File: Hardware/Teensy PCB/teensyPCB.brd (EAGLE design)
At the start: 100 x 50 mm, 14 parts, among them U2 USD-SOCKETNEW

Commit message: Created library component for digipot
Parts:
- added U$5: DIGIPOT, DigiPot:SOT23-8L
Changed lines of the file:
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@@
 <?xml version="1.0" encoding="utf-8"?>
 <!DOCTYPE eagle SYSTEM "eagle.dtd">
-<eagle version="7.4.0">
+<eagle version="7.2.0">
 <drawing>
 <settings>
@@
 <layers>
 <layer number="1" name="Top" color="4" fill="1" visible="yes" active="yes"/>
+<layer number="2" name="Route2" color="1" fill="3" visible="no" active="no"/>
+<layer number="3" name="Route3" color="4" fill="3" visible="no" active="no"/>
+<layer number="4" name="Route4" color="1" fill="4" visible="no" active="no"/>
+<layer number="5" name="Route5" color="4" fill="4" visible="no" active="no"/>
+<layer number="6" name="Route6" color="1" fill="8" visible="no" active="no"/>
+<layer number="7" name="Route7" color="4" fill="8" visible="no" active="no"/>
+<layer number="8" name="Route8" color="1" fill="2" visible="no" active="no"/>
+<layer number="9" name="Route9" color="4" fill="2" visible="no" active="no"/>
+<layer number="10" name="Route10" color="1" fill="7" visible="no" active="no"/>
+<layer number="11" name="Route11" color="4" fill="7" visible="no" active="no"/>
+<layer number="12" name="Route12" color="1" fill="5" visible="no" active="no"/>
+<layer number="13" name="Route13" color="4" fill="5" visible="no" active="no"/>
+<layer number="14" name="Route14" color="1" fill="6" visible="no" active="no"/>
+<layer number="15" name="Route15" color="4" fill="6" visible="no" active="no"/>
 <layer number="16" name="Bottom" color="1" fill="1" visible="yes" active="yes"/>
 <layer number="17" name="Pads" color="2" fill="1" visible="yes" active="yes"/>
@@
 <element name="U2" library="SparkFun-Connectors" package="MICRO-SD-SOCKET-PP" value="USD-SOCKETNEW" x="43.71" y="21.59"/>
 <element name="J_ULTRASONIC_2" library="HC-SR04" package="HC-SR04_FOOTPRINT" value="HC-SR04" x="43.77" y="8.2" rot="R90"/>
+<element name="U$5" library="DigiPot" package="SOT23-8L" value="DIGIPOT" x="-4" y="2"/>
 </elements>
 <signals>

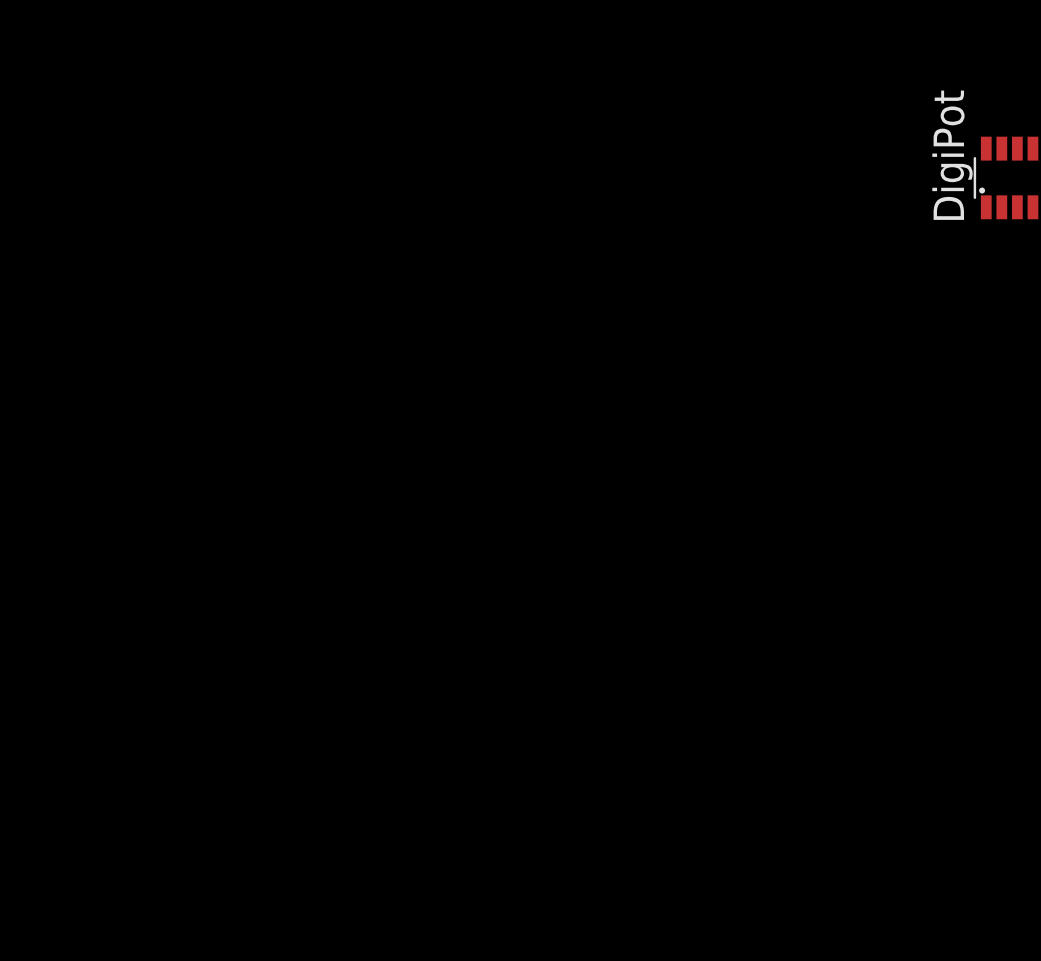
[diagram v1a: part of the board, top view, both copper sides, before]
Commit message: Wired digipot, added push buttons with voltage debounce, updated audio amplifier
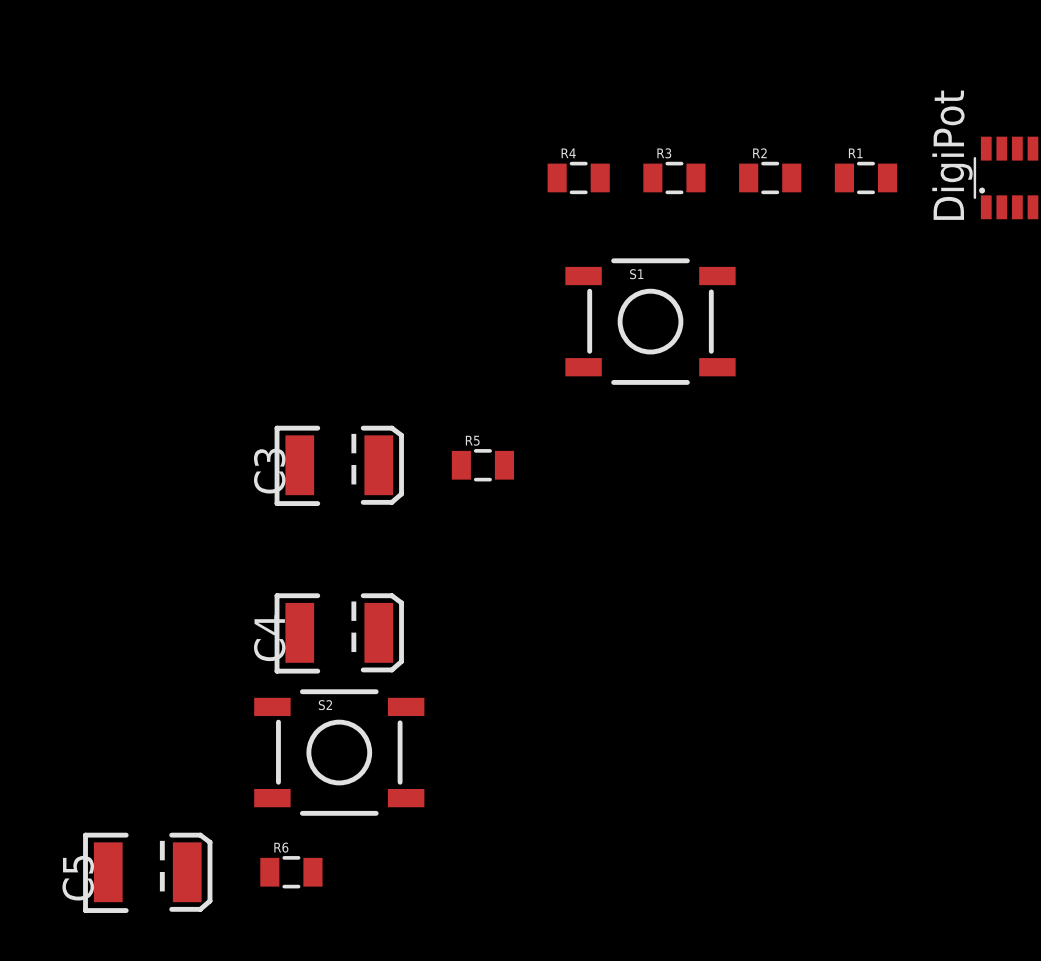
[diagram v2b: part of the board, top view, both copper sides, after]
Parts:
- added C3, C4: 100nF, SparkFun-Capacitors:EIA3528
- added C5: 10uF, SparkFun-Capacitors:EIA3528
- added R1, R2, R3, R4: 4.7k, SparkFun-Resistors:0805
- added R5, R6: 10k, SparkFun-Resistors:0805
- added S1, S2: TAC_SWITCHSMD, SparkFun-Retired:TACTILE-SWITCH-SMD
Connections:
- removed net VUSB: U$1.VUSB
- new net N$2: C4.C, R6.2, S2.3, S2.4, U$1.A11
- new net N$3: C5.C, U$5.A
- new net N$9: C3.C, R5.2, S1.3, S1.4, U$1.A12
- new net SW: U$1.A13, U$4.SW
- new net WOUT: C2.A, U$5.W
- net 5V: now also C3.A, C4.A, R1.2, R2.2, R3.2, R4.2, S1.1, S1.2, S2.1, S2.2, U$1.VUSB, U$5.VDD
- net DAC: now also C5.A; no longer C2.A
- net GND: now also R5.1, R6.1, U$5.AD0, U$5.B, U$5.GND
- net SCL0: now also R2.1, U$5.SCL
- net SCL1: now also R4.1
- net SDA0: now also R1.1, U$5.SDA
- net SDA1: now also R3.1
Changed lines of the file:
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@@
 <element name="J_ULTRASONIC_2" library="HC-SR04" package="HC-SR04_FOOTPRINT" value="HC-SR04" x="43.77" y="8.2" rot="R90"/>
 <element name="U$5" library="DigiPot" package="SOT23-8L" value="DIGIPOT" x="-4" y="2"/>
+<element name="R1" library="SparkFun-Resistors" package="0805" value="4.7k" x="-10" y="2"/>
+<element name="R2" library="SparkFun-Resistors" package="0805" value="4.7k" x="-14" y="2"/>
+<element name="R3" library="SparkFun-Resistors" package="0805" value="4.7k" x="-18" y="2"/>
+<element name="R4" library="SparkFun-Resistors" package="0805" value="4.7k" x="-22" y="2"/>
+<element name="S1" library="SparkFun-Retired" package="TACTILE-SWITCH-SMD" value="TAC_SWITCHSMD" x="-19" y="-4">
+<attribute name="PROD_ID" value="SWCH-08247" x="-19" y="-4" size="1.778" layer="27" display="off"/>
+</element>
+<element name="R5" library="SparkFun-Resistors" package="0805" value="10k" x="-26" y="-10"/>
+<element name="C3" library="SparkFun-Capacitors" package="EIA3528" value="100nF" x="-32" y="-10"/>
+<element name="S2" library="SparkFun-Retired" package="TACTILE-SWITCH-SMD" value="TAC_SWITCHSMD" x="-32" y="-22">
+<attribute name="PROD_ID" value="SWCH-08247" x="-32" y="-15" size="1.778" layer="27" display="off"/>
+</element>
+<element name="R6" library="SparkFun-Resistors" package="0805" value="10k" x="-34" y="-27"/>
+<element name="C4" library="SparkFun-Capacitors" package="EIA3528" value="100nF" x="-32" y="-17"/>
+<element name="C5" library="SparkFun-Capacitors" package="EIA3528" value="10uF" x="-40" y="-27"/>
 </elements>
 <signals>
@@
 <signal name="AREF">
 <contactref element="U$1" pad="AREF"/>
-</signal>
-<signal name="VUSB">
-<contactref element="U$1" pad="VUSB"/>
 </signal>
 <signal name="GND">
@@
 <contactref element="U$1" pad="GND2"/>
 <contactref element="U$1" pad="GND1"/>
+<contactref element="U$5" pad="B"/>
+<contactref element="U$5" pad="AD0"/>
+<contactref element="U$5" pad="GND"/>
+<contactref element="R5" pad="1"/>
+<contactref element="R6" pad="1"/>
 <wire x1="66.2" y1="25.21" x2="79.2" y2="45.12" width="0" layer="19" extent="1-1"/>
 <wire x1="54.8" y1="29.37" x2="66.2" y2="25.21" width="0" layer="19" extent="1-1"/>
@@
 <wire x1="92.02" y1="3.13" x2="86.94" y2="3.13" width="0" layer="19" extent="1-1"/>
 <wire x1="10.92" y1="44.7" x2="40.27" y2="32.49" width="0" layer="19" extent="1-1"/>
+<wire x1="-3.675" y1="3.225" x2="39.99" y2="3.47" width="0" layer="19" extent="1-1"/>
+<wire x1="-4.325" y1="3.225" x2="-3.675" y2="3.225" width="0" layer="19" extent="1-1"/>
+<wire x1="-3.675" y1="0.775" x2="-3.675" y2="3.225" width="0" layer="19" extent="1-1"/>
+<wire x1="-26.9" y1="-10" x2="-3.675" y2="0.775" width="0" layer="19" extent="1-1"/>
+<wire x1="-34.9" y1="-27" x2="-26.9" y2="-10" width="0" layer="19" extent="1-1"/>
 </signal>
 <signal name="3.3V">
@@
 <signal name="5V">
 <contactref element="TOBALANCE" pad="6"/>
+<contactref element="J_ULTRASONIC_1" pad="VCC"/>
+<contactref element="J_ULTRASONIC_2" pad="VCC"/>
+<contactref element="U$5" pad="VDD"/>
+<contactref element="R4" pad="2"/>
+<contactref element="R3" pad="2"/>
+<contactref element="R1" pad="2"/>
+<contactref element="R2" pad="2"/>
+<contactref element="S1" pad="1"/>
+<contactref element="C3" pad="A"/>
+<contactref element="S1" pad="2"/>
+<contactref element="C4" pad="A"/>
+<contactref element="S2" pad="2"/>
+<contactref element="S2" pad="1"/>
+<contactref element="U$1" pad="VUSB"/>
 <contactref element="U$4" pad="+5V"/>
 <contactref element="C1" pad="A"/>
-<contactref element="J_ULTRASONIC_1" pad="VCC"/>
-<contactref element="J_ULTRASONIC_2" pad="VCC"/>
+<wire x1="69.5" y1="25.21" x2="59.88" y2="44.61" width="0" layer="19" extent="1-1"/>
 <wire x1="65.15" y1="3.246" x2="69.5" y2="25.21" width="0" layer="19" extent="1-1"/>
 <wire x1="81.86" y1="3.13" x2="65.15" y2="3.246" width="0" layer="19" extent="1-1"/>
 <wire x1="47.61" y1="3.47" x2="65.15" y2="3.246" width="0" layer="19" extent="1-1"/>
 <wire x1="47.58" y1="8.2" x2="47.61" y2="3.47" width="0" layer="19" extent="1-1"/>
+<wire x1="-4.325" y1="0.775" x2="47.61" y2="3.47" width="0" layer="19" extent="1-1"/>
+<wire x1="-9.1" y1="2" x2="-4.325" y2="0.775" width="0" layer="19" extent="1-1"/>
+<wire x1="-13.1" y1="2" x2="-9.1" y2="2" width="0" layer="19" extent="1-1"/>
+<wire x1="-17.1" y1="2" x2="-13.1" y2="2" width="0" layer="19" extent="1-1"/>
+<wire x1="-21.1" y1="2" x2="-17.1" y2="2" width="0" layer="19" extent="1-1"/>
+<wire x1="-21.794" y1="-2.095" x2="-21.1" y2="2" width="0" layer="19" extent="1-1"/>
+<wire x1="-16.206" y1="-2.095" x2="-17.1" y2="2" width="0" layer="19" extent="1-1"/>
+<wire x1="-30.35" y1="-10" x2="-21.794" y2="-2.095" width="0" layer="19" extent="1-1"/>
+<wire x1="-30.35" y1="-17" x2="-30.35" y2="-10" width="0" layer="19" extent="1-1"/>
+<wire x1="-29.206" y1="-20.095" x2="-30.35" y2="-17" width="0" layer="19" extent="1-1"/>
+<wire x1="-34.794" y1="-20.095" x2="-30.35" y2="-17" width="0" layer="19" extent="1-1"/>
 </signal>
 <signal name="ARDUINO_RX">
@@
 <contactref element="U$1" pad="18/A4"/>
 <contactref element="U$2" pad="SDA"/>
+<contactref element="U$5" pad="SDA"/>
+<contactref element="R1" pad="1"/>
 <wire x1="62.42" y1="26.83" x2="81.74" y2="45.12" width="0" layer="19" extent="1-1"/>
+<wire x1="-3.025" y1="3.225" x2="62.42" y2="26.83" width="0" layer="19" extent="1-1"/>
+<wire x1="-10.9" y1="2" x2="-3.025" y2="3.225" width="0" layer="19" extent="1-1"/>
 </signal>
 <signal name="SCL0">
 <contactref element="U$1" pad="19/A5"/>
 <contactref element="U$2" pad="SCL"/>
+<contactref element="U$5" pad="SCL"/>
+<contactref element="R2" pad="1"/>
 <wire x1="62.42" y1="29.37" x2="84.28" y2="45.12" width="0" layer="19" extent="1-1"/>
+<wire x1="-3.025" y1="0.775" x2="62.42" y2="29.37" width="0" layer="19" extent="1-1"/>
+<wire x1="-14.9" y1="2" x2="-3.025" y2="0.775" width="0" layer="19" extent="1-1"/>
 </signal>
 <signal name="SDA1">
 <contactref element="U$3" pad="SDA"/>
 <contactref element="U$1" pad="30"/>
+<contactref element="R3" pad="1"/>
 <wire x1="13.46" y1="44.7" x2="57.34" y2="19.21" width="0" layer="19" extent="1-1"/>
+<wire x1="-18.9" y1="2" x2="13.46" y2="44.7" width="0" layer="19" extent="1-1"/>
 </signal>
 <signal name="SCL1">
 <contactref element="U$3" pad="SCL"/>
 <contactref element="U$1" pad="29"/>
+<contactref element="R4" pad="1"/>
 <wire x1="16" y1="44.7" x2="57.34" y2="16.67" width="0" layer="19" extent="1-1"/>
+<wire x1="-22.9" y1="2" x2="16" y2="44.7" width="0" layer="19" extent="1-1"/>
 </signal>
 <signal name="N$1">
@@
 </signal>
 <signal name="DAC">
-<contactref element="C2" pad="A"/>
 <contactref element="U$1" pad="RESET/DAC"/>
-<wire x1="59.88" y1="14.13" x2="69.5" y2="30.13" width="0" layer="19" extent="1-1"/>
+<contactref element="C5" pad="A"/>
+<wire x1="-38.35" y1="-27" x2="59.88" y2="14.13" width="0" layer="19" extent="1-1"/>
 </signal>
 <signal name="N$5">
@@
 <wire x1="45.04" y1="8.2" x2="62.42" y2="39.53" width="0" layer="19" extent="1-1"/>
 </signal>
+<signal name="WOUT">
+<contactref element="U$5" pad="W"/>
+<contactref element="C2" pad="A"/>
+<wire x1="-4.975" y1="0.775" x2="69.5" y2="30.13" width="0" layer="19" extent="1-1"/>
+</signal>
+<signal name="SW">
+<contactref element="U$1" pad="A13"/>
+<contactref element="U$4" pad="SW"/>
+<wire x1="84.4" y1="3.13" x2="57.34" y2="31.91" width="0" layer="19" extent="1-1"/>
+</signal>
+<signal name="N$9">
+<contactref element="S1" pad="3"/>
+<contactref element="S1" pad="4"/>
+<contactref element="R5" pad="2"/>
+<contactref element="C3" pad="C"/>
+<contactref element="U$1" pad="A12"/>
+<wire x1="-16.206" y1="-5.905" x2="54.8" y2="31.91" width="0" layer="19" extent="1-1"/>
+<wire x1="-21.794" y1="-5.905" x2="-16.206" y2="-5.905" width="0" layer="19" extent="1-1"/>
+<wire x1="-25.1" y1="-10" x2="-21.794" y2="-5.905" width="0" layer="19" extent="1-1"/>
+<wire x1="-33.65" y1="-10" x2="-25.1" y2="-10" width="0" layer="19" extent="1-1"/>
+</signal>
+<signal name="N$2">
+<contactref element="S2" pad="4"/>
+<contactref element="S2" pad="3"/>
+<contactref element="R6" pad="2"/>
+<contactref element="C4" pad="C"/>
+<contactref element="U$1" pad="A11"/>
+<wire x1="-29.206" y1="-23.905" x2="59.88" y2="34.45" width="0" layer="19" extent="1-1"/>
+<wire x1="-33.1" y1="-27" x2="-29.206" y2="-23.905" width="0" layer="19" extent="1-1"/>
+<wire x1="-34.794" y1="-23.905" x2="-33.1" y2="-27" width="0" layer="19" extent="1-1"/>
+<wire x1="-33.65" y1="-17" x2="-34.794" y2="-23.905" width="0" layer="19" extent="1-1"/>
+</signal>
+<signal name="N$3">
+<contactref element="U$5" pad="A"/>
+<contactref element="C5" pad="C"/>
+<wire x1="-4.975" y1="3.225" x2="-41.65" y2="-27" width="0" layer="19" extent="1-1"/>
+</signal>
 </signals>

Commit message: fixed error
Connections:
- new net VUSB: U$1.VUSB
- net 5V: no longer U$1.VUSB
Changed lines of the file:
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@@
 <contactref element="S2" pad="2"/>
 <contactref element="S2" pad="1"/>
-<contactref element="U$1" pad="VUSB"/>
 <contactref element="U$4" pad="+5V"/>
 <contactref element="C1" pad="A"/>
-<wire x1="69.5" y1="25.21" x2="59.88" y2="44.61" width="0" layer="19" extent="1-1"/>
 <wire x1="65.15" y1="3.246" x2="69.5" y2="25.21" width="0" layer="19" extent="1-1"/>
 <wire x1="81.86" y1="3.13" x2="65.15" y2="3.246" width="0" layer="19" extent="1-1"/>
@@
 <wire x1="-4.975" y1="3.225" x2="-41.65" y2="-27" width="0" layer="19" extent="1-1"/>
 </signal>
+<signal name="VUSB">
+<contactref element="U$1" pad="VUSB"/>
+</signal>
 </signals>

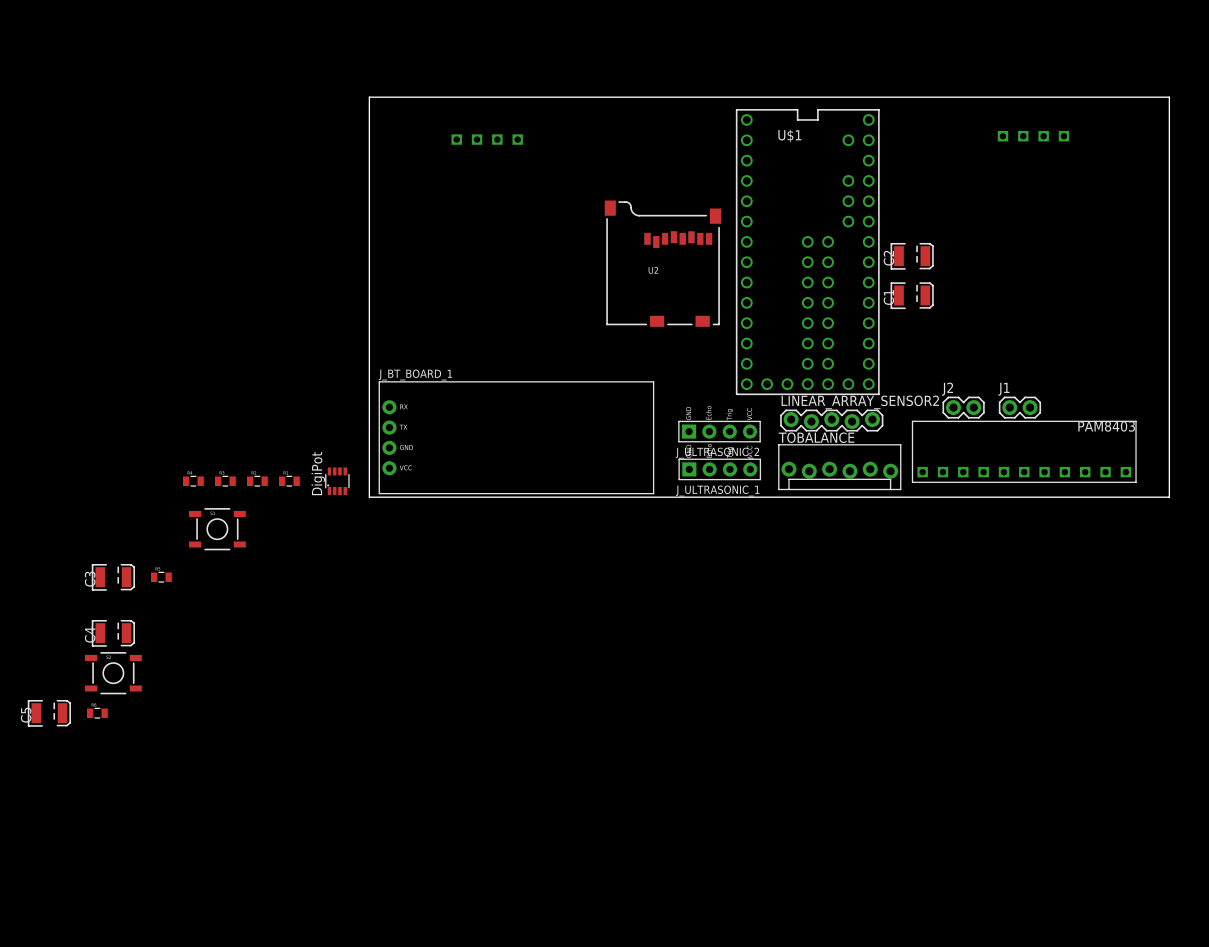
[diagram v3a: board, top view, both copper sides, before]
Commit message: Worked on board schematic, added coin cell slot
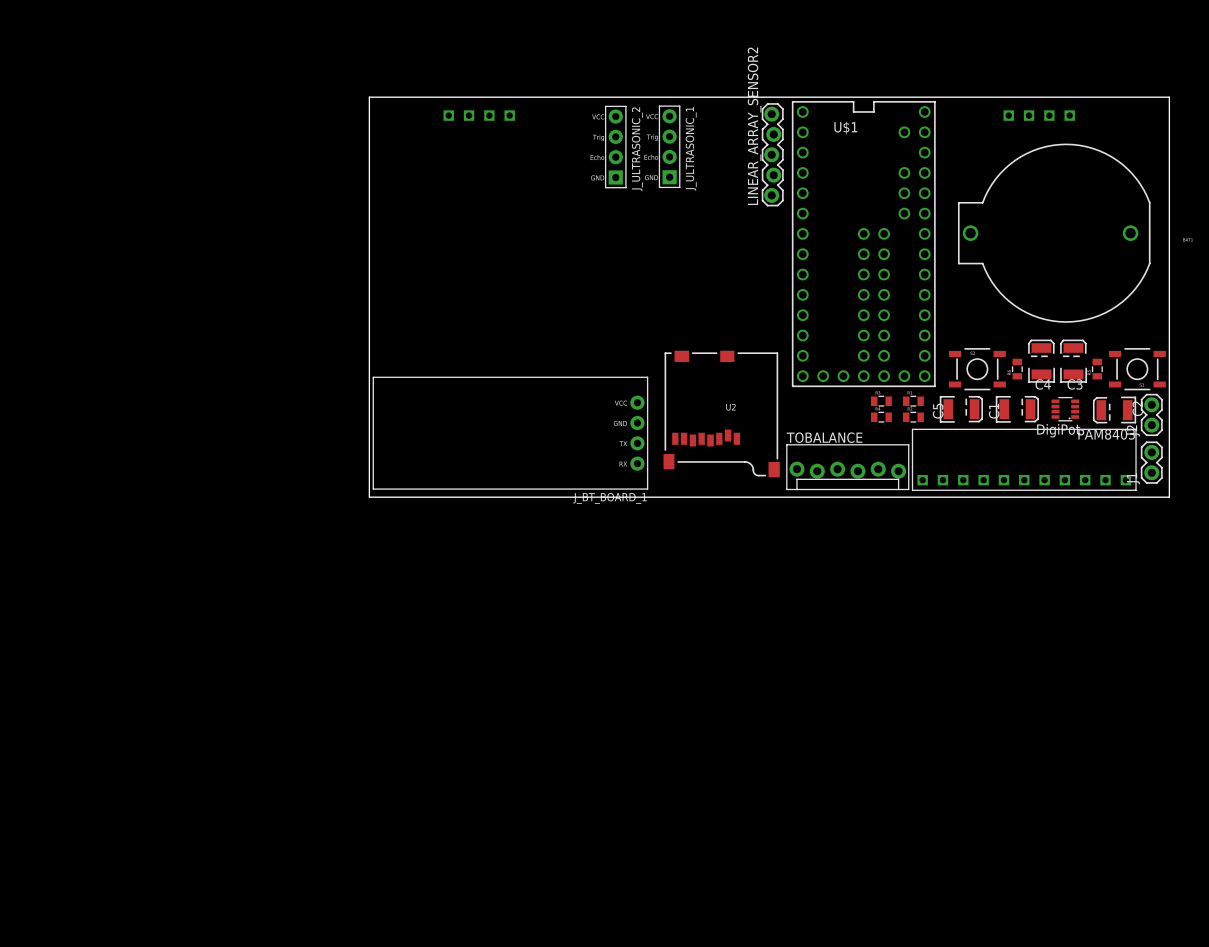
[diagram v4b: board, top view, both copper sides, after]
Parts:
- added BAT1: (no value), SparkFun-Electromechanical:BATTCOM_20MM_PTH
- moved C3 123.0 mm to (88.0, 17.0), turned to 90 degrees
- moved R6 122.8 mm to (81.0, 16.0), turned to 90 degrees
- moved C4 120.9 mm to (84.0, 17.0), turned to 90 degrees
- moved C5 120.2 mm to (74.0, 11.0)
- moved R5 119.9 mm to (91.0, 16.0), turned to 90 degrees
- moved S1 116.7 mm to (96.0, 16.0), turned to 180 degrees
- moved S2 114.5 mm to (76.0, 16.0)
- moved U$5 91.4 mm to (87.0, 11.0), turned to 90 degrees
- moved R4 86.4 mm to (64.0, 10.0)
- moved R3 82.6 mm to (64.0, 12.0)
- moved R2 82.4 mm to (68.0, 10.0)
- moved R1 78.6 mm to (68.0, 12.0)
- moved J_ULTRASONIC_1 40.8 mm to (37.5, 43.8), turned to 180 degrees
- moved J_ULTRASONIC_2 37.9 mm to (30.8, 43.8), turned to 180 degrees
- moved C2 31.8 mm to (93.2, 10.9), turned to 180 degrees
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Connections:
- net GND: now also BAT1.2
- net VBAT: now also BAT1.1
